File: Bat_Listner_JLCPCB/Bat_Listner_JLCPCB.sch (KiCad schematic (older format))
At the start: 48 parts, among them IC1 CD4024BM96, IC2 TL074IDR, IC3 MA40S4S, J2 B2B-PH-K-S_LF__SN_, J3 B2B-PH-K-S_LF__SN_, J4 B2B-PH-K-S_LF__SN_, J5 B2B-PH-K-S_LF__SN_, J6 STX-3200-3NB, Q1 BC817-40W,115

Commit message: completed wiring
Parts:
- removed C4: 220uF_E, Capacitor_SMD:CP_Elec_6.3x7.7, symbol Capacitor_JLC:220uF_E
- added C17, C18, C4: 100uF_E, Capacitor_SMD:CP_Elec_6.3x7.7, symbol Capacitor_JLC:100uF_E
- added R13, R14: 68k, Resistor_SMD:R_0402_1005Metric, symbol Resistor_JLC:68k
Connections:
- net labels added: 1, 11, 2, 3, 4
- wire segments 184 -> 208
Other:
- moved on the sheet: C14, C16, C5, C7, D1, D2, D3, D4, IC1, J2, J3, J4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

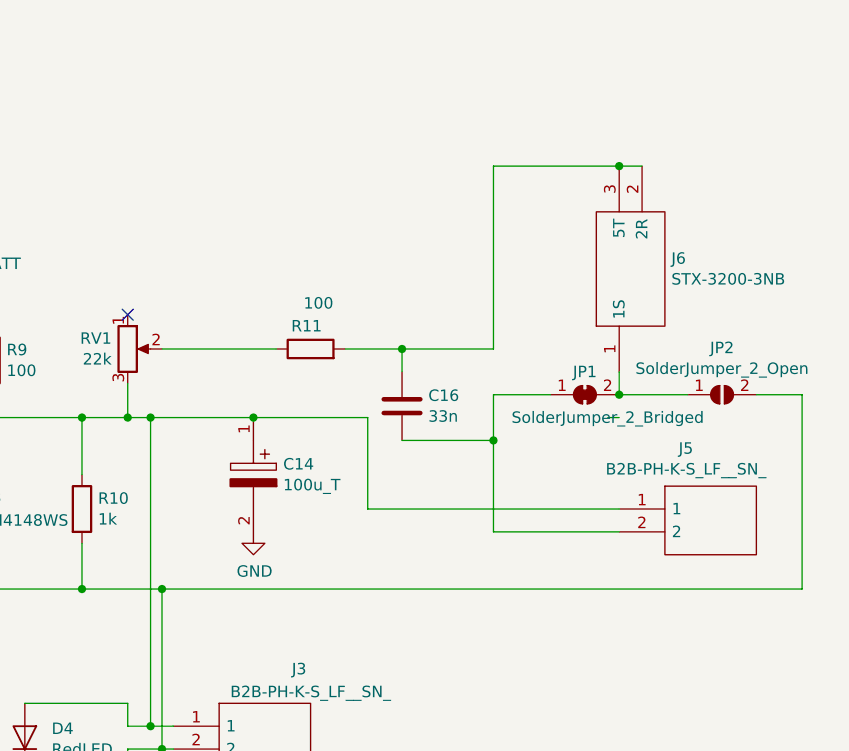
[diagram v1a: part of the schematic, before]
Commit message: updated pcb to fix audio jack
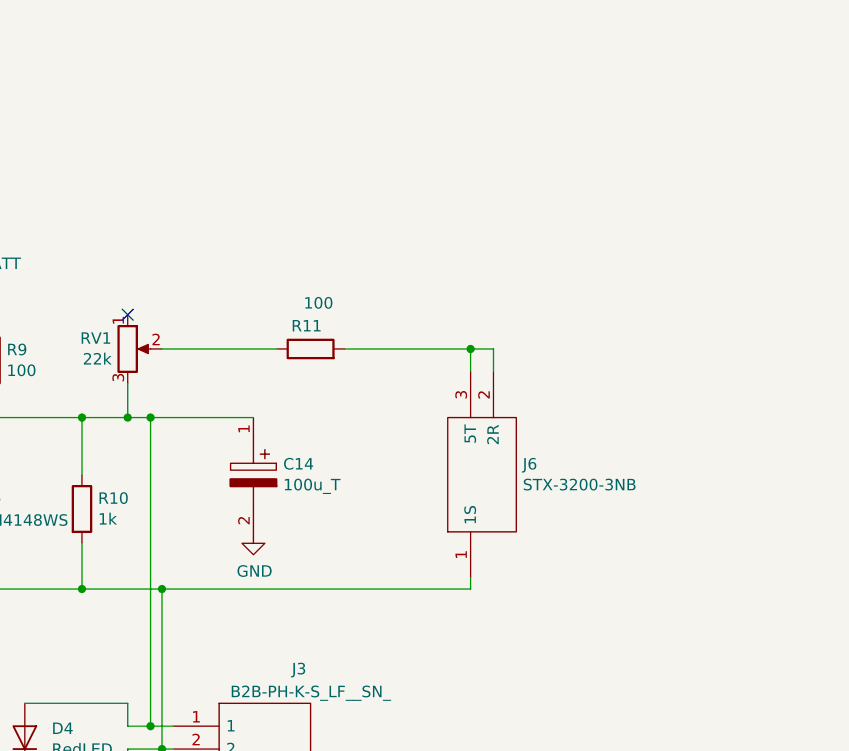
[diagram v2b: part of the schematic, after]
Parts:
- removed C16: 33n, Capacitor_SMD:C_0402_1005Metric, symbol Capacitor_JLC:33n
- removed J5: B2B-PH-K-S_LF__SN_, SamacSys_Parts:SHDR2W50P0X200_1X2_590X450X600P, symbol SamacSys_Parts:B2B-PH-K-S_LF__SN_
- removed JP1: SolderJumper_2_Bridged, Jumper:SolderJumper-2_P1.3mm_Bridged_Pad1.0x1.5mm, symbol Jumper:SolderJumper_2_Bridged
- removed JP2: SolderJumper_2_Open, Jumper:SolderJumper-2_P1.3mm_Open_Pad1.0x1.5mm, symbol Jumper:SolderJumper_2_Open
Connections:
- net at D3.2 (A), D4.1 (K), J3.2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: now also J6.1 (1S)
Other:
- moved on the sheet: J6
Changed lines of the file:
@@
-$EndComp
-$Comp
-L Capacitor_JLC:33n C16
-U 1 1 5FAB6F92
-P 13050 6500
-F 0 "C16" H 13165 6546 50  0000 L CNN
-F 1 "33n" H 13165 6455 50  0000 L CNN
-F 2 "Capacitor_SMD:C_0402_1005Metric" H 13088 6350 50  0001 C CNN
-F 3 "~" H 13050 6500 50  0001 C CNN
-F 4 "X7R" H 13050 6500 50  0001 C CNN "Type"
-F 5 "C1585" H 13050 6500 50  0001 C CNN "LCSC"
-	1    13050 6500
-	1    0    0    -1
 $EndComp
 $Comp
@@
 Wire Wire Line
 	12000 6250 12500 6250
-Wire Wire Line
-	13450 6250 13050 6250
-Wire Wire Line
-	13050 6350 13050 6250
-Connection ~ 13050 6250
-Wire Wire Line
-	13050 6250 12800 6250
 Connection ~ 11650 7300
 $Comp
@@
 $EndComp
 Wire Wire Line
-	13450 6650 13050 6650
-$Comp
-L SamacSys_Parts:B2B-PH-K-S_LF__SN_ J5
-U 1 1 5FF5FE07
-P 14000 6950
-F 0 "J5" H 14292 7215 50  0000 C CNN
-F 1 "B2B-PH-K-S_LF__SN_" H 14292 7124 50  0000 C CNN
-F 2 "SamacSys_Parts:SHDR2W50P0X200_1X2_590X450X600P" H 14650 7050 50  0001 L CNN
-F 3 "http://www.jst-mfg.com/product/pdf/eng/ePH.pdf" H 14650 6950 50  0001 L CNN
-F 4 "PH-2.0mm Header top entry 2 way JST PH Series, Series Number B2B, 2mm Pitch 2 Way 1 Row Straight PCB Header, Through Hole Termination, 2A" H 14650 6850 50  0001 L CNN "Description"
-F 5 "6" H 14650 6750 50  0001 L CNN "Height"
-F 6 "JST (JAPAN SOLDERLESS TERMINALS)" H 14650 6650 50  0001 L CNN "Manufacturer_Name"
-F 7 "B2B-PH-K-S(LF)(SN)" H 14650 6550 50  0001 L CNN "Manufacturer_Part_Number"
-F 8 "8201422P" H 14650 6250 50  0001 L CNN "RS Part Number"
-F 9 "http://uk.rs-online.com/web/p/products/8201422P" H 14650 6150 50  0001 L CNN "RS Price/Stock"
-	1    14000 6950
-	1    0    0    -1
-$EndComp
-Wire Wire Line
-	13450 7050 14000 7050
-Wire Wire Line
-	13450 6650 13450 7050
-Wire Wire Line
-	12400 6550 12900 6550
-Wire Wire Line
-	12900 6550 12900 6950
-Wire Wire Line
-	12900 6950 14000 6950
-Connection ~ 12400 6550
-Wire Wire Line
 	11850 7900 11850 7800
 Wire Wire Line
@@
 Wire Wire Line
 	12000 8000 12050 8000
-Connection ~ 12000 7300
 $Comp
 L SamacSys_Parts:STX-3200-3NB J6
 U 1 1 5FFD539A
-P 14000 6350
-F 0 "J6" V 14496 6122 50  0000 R CNN
-F 1 "STX-3200-3NB" V 14405 6122 50  0000 R CNN
-F 2 "SamacSys_Parts:STX32003NB" H 14750 6450 50  0001 L CNN
-F 3 "https://componentsearchengine.com/Datasheets/1/STX-3200-3NB.pdf" H 14750 6350 50  0001 L CNN
-F 4 "Phone Connectors 3.5mm PCB W/BACKPLTE NON-THREADED" H 14750 6250 50  0001 L CNN "Description"
-F 5 "11.35" H 14750 6150 50  0001 L CNN "Height"
-F 6 "806-STX-3200-3NB" H 14750 6050 50  0001 L CNN "Mouser Part Number"
-F 7 "https://www.mouser.com/Search/Refine.aspx?Keyword=806-STX-3200-3NB" H 14750 5950 50  0001 L CNN "Mouser Price/Stock"
-F 8 "Kycon" H 14750 5850 50  0001 L CNN "Manufacturer_Name"
-F 9 "STX-3200-3NB" H 14750 5750 50  0001 L CNN "Manufacturer_Part_Number"
-	1    14000 6350
+P 13350 7250
+F 0 "J6" V 13846 7022 50  0000 R CNN
+F 1 "STX-3200-3NB" V 13755 7022 50  0000 R CNN
+F 2 "SamacSys_Parts:STX32003NB" H 14100 7350 50  0001 L CNN
+F 3 "https://componentsearchengine.com/Datasheets/1/STX-3200-3NB.pdf" H 14100 7250 50  0001 L CNN
+F 4 "Phone Connectors 3.5mm PCB W/BACKPLTE NON-THREADED" H 14100 7150 50  0001 L CNN "Description"
+F 5 "11.35" H 14100 7050 50  0001 L CNN "Height"
+F 6 "806-STX-3200-3NB" H 14100 6950 50  0001 L CNN "Mouser Part Number"
+F 7 "https://www.mouser.com/Search/Refine.aspx?Keyword=806-STX-3200-3NB" H 14100 6850 50  0001 L CNN "Mouser Price/Stock"
+F 8 "Kycon" H 14100 6750 50  0001 L CNN "Manufacturer_Name"
+F 9 "STX-3200-3NB" H 14100 6650 50  0001 L CNN "Manufacturer_Part_Number"
+	1    13350 7250
 	0    -1   -1   0
 $EndComp
-Wire Wire Line
-	14100 5450 14000 5450
-Wire Wire Line
-	13450 5450 13450 6250
-Connection ~ 14000 5450
-Wire Wire Line
-	14000 5450 13450 5450
-$Comp
-L Jumper:SolderJumper_2_Bridged JP1
-U 1 1 5FFFC3DD
-P 13850 6450
-F 0 "JP1" H 13850 6550 50  0000 C CNN
-F 1 "SolderJumper_2_Bridged" H 13950 6350 50  0000 C CNN
-F 2 "Jumper:SolderJumper-2_P1.3mm_Bridged_Pad1.0x1.5mm" H 13850 6450 50  0001 C CNN
-F 3 "~" H 13850 6450 50  0001 C CNN
-	1    13850 6450
-	1    0    0    -1
-$EndComp
-Wire Wire Line
-	14000 6350 14000 6450
-Wire Wire Line
-	14000 6550 13950 6550
-Connection ~ 13450 6650
-Wire Wire Line
-	13700 6450 13450 6450
-Wire Wire Line
-	13450 6450 13450 6650
-$Comp
-L Jumper:SolderJumper_2_Open JP2
-U 1 1 6001631F
-P 14450 6450
-F 0 "JP2" H 14450 6655 50  0000 C CNN
-F 1 "SolderJumper_2_Open" H 14450 6564 50  0000 C CNN
-F 2 "Jumper:SolderJumper-2_P1.3mm_Open_Pad1.0x1.5mm" H 14450 6450 50  0001 C CNN
-F 3 "~" H 14450 6450 50  0001 C CNN
-	1    14450 6450
-	1    0    0    -1
-$EndComp
-Wire Wire Line
-	14000 6450 14300 6450
-Connection ~ 14000 6450
-Wire Wire Line
-	14800 7300 14800 6450
-Wire Wire Line
-	14800 6450 14600 6450
-Wire Wire Line
-	12000 7300 14800 7300
 Wire Wire Line
 	4800 3050 4700 3050
@@
 Wire Wire Line
 	2150 9500 1850 9500
+Wire Wire Line
+	12800 6250 13350 6250
+Connection ~ 13350 6250
+Wire Wire Line
+	13350 6250 13450 6250
+Wire Wire Line
+	13350 7300 12000 7300
+Connection ~ 12000 7300
+Wire Wire Line
+	13350 7250 13350 7300
+Wire Wire Line
+	13350 6250 13350 6350
+Wire Wire Line
+	13450 6250 13450 6350
 $EndSCHEMATC

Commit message: wip
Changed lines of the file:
@@
 Text GLabel 13050 3600 0    50   Input ~ 0
 3
-Text GLabel 13050 3700 0    50   Input ~ 0
-4
-Wire Wire Line
-	13050 3700 13300 3700
 Wire Wire Line
 	13300 3600 13050 3600
@@
 Wire Wire Line
 	13300 3400 13050 3400
-Text GLabel 3000 7500 2    50   Input ~ 0
-4
-Wire Wire Line
-	3000 7500 2750 7500
-Connection ~ 2750 7500
 Text GLabel 3000 8900 2    50   Input ~ 0
 11
@@
 Wire Wire Line
 	13450 6250 13450 6350
+$Comp
+L power:+BATT #PWR0114
+U 1 1 601F503E
+P 12750 3600
+F 0 "#PWR0114" H 12750 3450 50  0001 C CNN
+F 1 "+BATT" H 12765 3773 50  0000 C CNN
+F 2 "" H 12750 3600 50  0001 C CNN
+F 3 "" H 12750 3600 50  0001 C CNN
+	1    12750 3600
+	1    0    0    -1
+$EndComp
+Wire Wire Line
+	12750 3600 12750 3700
+Wire Wire Line
+	12750 3700 13300 3700
 $EndSCHEMATC

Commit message: updated design
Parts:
- removed J2, J3, J4: B2B-PH-K-S_LF__SN_, SamacSys_Parts:SHDR2W50P0X200_1X2_590X450X600P, symbol SamacSys_Parts:B2B-PH-K-S_LF__SN_
- removed J6: STX-3200-3NB, SamacSys_Parts:STX32003NB, symbol SamacSys_Parts:STX-3200-3NB
- removed RV1, RV2: 22k, Potentiometer_THT:Potentiometer_Bourns_3296W_Vertical, symbol Device:R_POT
- added J1, J2, J4: PH-2W, SHDRRA2W50P0X200_1X2_600X760X510P, symbol Connector_JLC:PH-2W
- added J3: WQP-PJ313D, C18167, symbol Connector_JLC:WQP-PJ313D
- added RV1, RV2: 10K_RV, 3314J-1, symbol Resistor_JLC:10K_RV
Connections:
- net +BATT: now also J4.1
- net 13: now also RV1.1, RV1.2
- net GND: now also J1.2, J4.2; no longer IC2.11 (VCC-)
- net at C13.2: now also RV1.3
- net at D3.2 (A), D4.1 (K), Q1.3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: now also J2.2, J3.A2 (S2)
- net at D1.1 (K), R1.2: now also J1.1
- net at C14.1, D3.1 (K), D4.2 (A)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: now also J2.1, RV2.3
- net at R11.1: now also RV2.2
- net at R11.2: now also J3.A1 (T2), J3.A3 (R)
- new net 11: IC2.11 (VCC-)
- no-connect marks 7 -> 9

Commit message: finished
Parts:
- added JP1, JP2: Jumper_2_Bridged, Jumper:SolderJumper-2_P1.3mm_Bridged_Pad1.0x1.5mm, symbol Jumper:Jumper_2_Bridged
- added LS1: MLT-7525, MLT7525, symbol Misc_JLC:MLT-7525
- J1: renamed from J4; value PH-2W -> PH-2V; footprint SHDRRA2W50P0X200_1X2_600X760X510P -> SHDR2W52P0X200_1X2_600X460X630P; symbol Connector_JLC:PH-2W -> Connector_JLC:PH-2V; Description Headers & Wire Housings Thruhole right angle backlight conn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 -> Wire To Board / Wire To Wire Connector Through Hole RoHS; Height 5.1 -> 6.3; LCSC C225207 -> C146082; Manufacturer_Name Newhaven Display -> BOOMELE(Boom Precision Elec); Manufacturer_Part_Number A2001WR-2P Thru-hole -> PH-2AK
- J2: renamed from J1; value PH-2W -> PH-2V; footprint SHDRRA2W50P0X200_1X2_600X760X510P -> SHDR2W52P0X200_1X2_600X460X630P; symbol Connector_JLC:PH-2W -> Connector_JLC:PH-2V; Description Headers & Wire Housings Thruhole right angle backlight conn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 -> Wire To Board / Wire To Wire Connector Through Hole RoHS; Height 5.1 -> 6.3; LCSC C225207 -> C146082; Manufacturer_Name Newhaven Display -> BOOMELE(Boom Precision Elec); Manufacturer_Part_Number A2001WR-2P Thru-hole -> PH-2AK
- J4: renamed from J2; value PH-2W -> PH-2V; footprint SHDRRA2W50P0X200_1X2_600X760X510P -> SHDR2W52P0X200_1X2_600X460X630P; symbol Connector_JLC:PH-2W -> Connector_JLC:PH-2V; Description Headers & Wire Housings Thruhole right angle backlight conn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 -> Wire To Board / Wire To Wire Connector Through Hole RoHS; Height 5.1 -> 6.3; LCSC C225207 -> C146082; Manufacturer_Name Newhaven Display -> BOOMELE(Boom Precision Elec); Manufacturer_Part_Number A2001WR-2P Thru-hole -> PH-2AK
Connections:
- net at AT1.2 (-INPUT), IC3.1: now also JP1.1 (A)
- net at AT1.3 (+INPUT), IC3.2: now also JP2.1 (A)
- new net: JP2.2 (B), LS1.1 (+LEAD)
- new net: JP1.2 (B), LS1.2 (-LEAD)
- no-connect marks 9 -> 11
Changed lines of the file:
@@
 	-1   0    0    -1
 $EndComp
-Wire Wire Line
-	2400 3800 2950 3800
-Wire Wire Line
-	2400 3700 2950 3700
 $Comp
 L personal:TestPoint TP1
@@
 NoConn ~ 13950 6900
 $Comp
-L Connector_JLC:PH-2W J2
+L Connector_JLC:PH-2V J4
 U 1 1 6032C940
 P 12050 7900
-F 0 "J2" H 12678 7896 50  0000 L CNN
-F 1 "PH-2W" H 12678 7805 50  0000 L CNN
-F 2 "SHDRRA2W50P0X200_1X2_600X760X510P" H 12700 8000 50  0001 L CNN
-F 3 "https://www.mouser.ca/datasheet/2/291/A2001-1532311.pdf" H 12700 7900 50  0001 L CNN
-F 4 "Headers & Wire Housings Thruhole right angle backlight connector" H 12700 7800 50  0001 L CNN "Description"
-F 5 "5.1" H 12700 7700 50  0001 L CNN "Height"
-F 6 "Newhaven Display" H 12700 7600 50  0001 L CNN "Manufacturer_Name"
-F 7 "A2001WR-2P Thru-hole" H 12700 7500 50  0001 L CNN "Manufacturer_Part_Number"
+F 0 "J4" H 12678 7896 50  0000 L CNN
+F 1 "PH-2V" H 12678 7805 50  0000 L CNN
+F 2 "SHDR2W52P0X200_1X2_600X460X630P" H 12700 8000 50  0001 L CNN
+F 3 "https://datasheet.lcsc.com/szlcsc/1811092130_BOOMELE-Boom-Precision-Elec-PH-2AK_C146082.pdf" H 12700 7900 50  0001 L CNN
+F 4 "Wire To Board / Wire To Wire Connector Through Hole RoHS" H 12700 7800 50  0001 L CNN "Description"
+F 5 "6.3" H 12700 7700 50  0001 L CNN "Height"
+F 6 "BOOMELE(Boom Precision Elec)" H 12700 7600 50  0001 L CNN "Manufacturer_Name"
+F 7 "PH-2AK" H 12700 7500 50  0001 L CNN "Manufacturer_Part_Number"
 F 8 "763-A2001WR2P" H 12700 7400 50  0001 L CNN "Mouser Part Number"
 F 9 "https://www.mouser.co.uk/ProductDetail/Newhaven-Display/A2001WR-2P-Thru-hole?qs=gZXFycFWdAPcYjIK7pURng%3D%3D" H 12700 7300 50  0001 L CNN "Mouser Price/Stock"
-F 10 "C225207" H 12050 7900 50  0001 C CNN "LCSC"
+F 10 "C146082" H 12050 7900 50  0001 C CNN "LCSC"
 	1    12050 7900
 	1    0    0    -1
 $EndComp
 $Comp
-L Connector_JLC:PH-2W J1
+L Connector_JLC:PH-2V J2
 U 1 1 6032DABE
 P 7050 8550
-F 0 "J1" H 7678 8546 50  0000 L CNN
-F 1 "PH-2W" H 7678 8455 50  0000 L CNN
-F 2 "SHDRRA2W50P0X200_1X2_600X760X510P" H 7700 8650 50  0001 L CNN
-F 3 "https://www.mouser.ca/datasheet/2/291/A2001-1532311.pdf" H 7700 8550 50  0001 L CNN
-F 4 "Headers & Wire Housings Thruhole right angle backlight connector" H 7700 8450 50  0001 L CNN "Description"
-F 5 "5.1" H 7700 8350 50  0001 L CNN "Height"
-F 6 "Newhaven Display" H 7700 8250 50  0001 L CNN "Manufacturer_Name"
-F 7 "A2001WR-2P Thru-hole" H 7700 8150 50  0001 L CNN "Manufacturer_Part_Number"
+F 0 "J2" H 7678 8546 50  0000 L CNN
+F 1 "PH-2V" H 7678 8455 50  0000 L CNN
+F 2 "SHDR2W52P0X200_1X2_600X460X630P" H 7700 8650 50  0001 L CNN
+F 3 "https://datasheet.lcsc.com/szlcsc/1811092130_BOOMELE-Boom-Precision-Elec-PH-2AK_C146082.pdf" H 7700 8550 50  0001 L CNN
+F 4 "Wire To Board / Wire To Wire Connector Through Hole RoHS" H 7700 8450 50  0001 L CNN "Description"
+F 5 "6.3" H 7700 8350 50  0001 L CNN "Height"
+F 6 "BOOMELE(Boom Precision Elec)" H 7700 8250 50  0001 L CNN "Manufacturer_Name"
+F 7 "PH-2AK" H 7700 8150 50  0001 L CNN "Manufacturer_Part_Number"
 F 8 "763-A2001WR2P" H 7700 8050 50  0001 L CNN "Mouser Part Number"
 F 9 "https://www.mouser.co.uk/ProductDetail/Newhaven-Display/A2001WR-2P-Thru-hole?qs=gZXFycFWdAPcYjIK7pURng%3D%3D" H 7700 7950 50  0001 L CNN "Mouser Price/Stock"
-F 10 "C225207" H 7050 8550 50  0001 C CNN "LCSC"
+F 10 "C146082" H 7050 8550 50  0001 C CNN "LCSC"
 	1    7050 8550
 	1    0    0    -1
@@
 $EndComp
 $Comp
-L Connector_JLC:PH-2W J4
+L Connector_JLC:PH-2V J1
 U 1 1 60369C79
 P 1800 8000
-F 0 "J4" H 2428 7996 50  0000 L CNN
-F 1 "PH-2W" H 2428 7905 50  0000 L CNN
-F 2 "SHDRRA2W50P0X200_1X2_600X760X510P" H 2450 8100 50  0001 L CNN
-F 3 "https://www.mouser.ca/datasheet/2/291/A2001-1532311.pdf" H 2450 8000 50  0001 L CNN
-F 4 "Headers & Wire Housings Thruhole right angle backlight connector" H 2450 7900 50  0001 L CNN "Description"
-F 5 "5.1" H 2450 7800 50  0001 L CNN "Height"
-F 6 "Newhaven Display" H 2450 7700 50  0001 L CNN "Manufacturer_Name"
-F 7 "A2001WR-2P Thru-hole" H 2450 7600 50  0001 L CNN "Manufacturer_Part_Number"
+F 0 "J1" H 2428 7996 50  0000 L CNN
+F 1 "PH-2V" H 2428 7905 50  0000 L CNN
+F 2 "SHDR2W52P0X200_1X2_600X460X630P" H 2450 8100 50  0001 L CNN
+F 3 "https://datasheet.lcsc.com/szlcsc/1811092130_BOOMELE-Boom-Precision-Elec-PH-2AK_C146082.pdf" H 2450 8000 50  0001 L CNN
+F 4 "Wire To Board / Wire To Wire Connector Through Hole RoHS" H 2450 7900 50  0001 L CNN "Description"
+F 5 "6.3" H 2450 7800 50  0001 L CNN "Height"
+F 6 "BOOMELE(Boom Precision Elec)" H 2450 7700 50  0001 L CNN "Manufacturer_Name"
+F 7 "PH-2AK" H 2450 7600 50  0001 L CNN "Manufacturer_Part_Number"
 F 8 "763-A2001WR2P" H 2450 7500 50  0001 L CNN "Mouser Part Number"
 F 9 "https://www.mouser.co.uk/ProductDetail/Newhaven-Display/A2001WR-2P-Thru-hole?qs=gZXFycFWdAPcYjIK7pURng%3D%3D" H 2450 7400 50  0001 L CNN "Mouser Price/Stock"
-F 10 "C225207" H 1800 8000 50  0001 C CNN "LCSC"
+F 10 "C146082" H 1800 8000 50  0001 C CNN "LCSC"
 	1    1800 8000
 	-1   0    0    -1
 $EndComp
+$Comp
+L Misc_JLC:MLT-7525 LS1
+U 1 1 60289092
+P 2400 4600
+F 0 "LS1" H 3050 4865 50  0000 C CNN
+F 1 "MLT-7525" H 3050 4774 50  0000 C CNN
+F 2 "MLT7525" H 3550 4700 50  0001 L CNN
+F 3 "https://datasheet.lcsc.com/szlcsc/Jiangsu-Huaneng-Elec-MLT-7525_C95299.pdf" H 3550 4600 50  0001 L CNN
+F 4 "Buzzers Magnetic NO 2700Hz 3.6V 2.5 ~ 4.5V 7.5mm x 7.5mm 7.5*7.5*2.5mm RoHS" H 3550 4500 50  0001 L CNN "Description"
+F 5 "2.5" H 3550 4400 50  0001 L CNN "Height"
+F 6 "Jiangsu Huaneng Elec" H 3550 4300 50  0001 L CNN "Manufacturer_Name"
+F 7 "MLT-7525" H 3550 4200 50  0001 L CNN "Manufacturer_Part_Number"
+F 8 "C95299" H 2400 4600 50  0001 C CNN "LCSC"
+	1    2400 4600
+	-1   0    0    1
+$EndComp
+Wire Wire Line
+	2400 4500 2500 4500
+NoConn ~ 1100 4400
+NoConn ~ 1100 4500
+$Comp
+L Jumper:Jumper_2_Bridged JP1
+U 1 1 602C0074
+P 2500 4100
+F 0 "JP1" V 2450 3800 50  0000 C CNN
+F 1 "Jumper_2_Bridged" V 2550 3700 50  0000 C CNN
+F 2 "Jumper:SolderJumper-2_P1.3mm_Bridged_Pad1.0x1.5mm" H 2500 4100 50  0001 C CNN
+F 3 "~" H 2500 4100 50  0001 C CNN
+	1    2500 4100
+	0    1    1    0
+$EndComp
+$Comp
+L Jumper:Jumper_2_Bridged JP2
+U 1 1 60380F00
+P 2650 4300
+F 0 "JP2" V 2600 3850 50  0000 C CNN
+F 1 "Jumper_2_Bridged" V 2700 3750 50  0000 C CNN
+F 2 "Jumper:SolderJumper-2_P1.3mm_Bridged_Pad1.0x1.5mm" H 2650 4300 50  0001 C CNN
+F 3 "~" H 2650 4300 50  0001 C CNN
+	1    2650 4300
+	0    1    1    0
+$EndComp
+Wire Wire Line
+	2500 4300 2500 4500
+Wire Wire Line
+	2650 4500 2650 4600
+Wire Wire Line
+	2400 4600 2650 4600
+Wire Wire Line
+	2400 3800 2650 3800
+Wire Wire Line
+	2400 3700 2500 3700
+Wire Wire Line
+	2500 3900 2500 3700
+Connection ~ 2500 3700
+Wire Wire Line
+	2500 3700 2950 3700
+Wire Wire Line
+	2650 3800 2650 4100
+Connection ~ 2650 3800
+Wire Wire Line
+	2650 3800 2950 3800
 $EndSCHEMATC
